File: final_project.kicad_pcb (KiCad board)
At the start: 2 copper layers, 21 parts, among them J1 Conn_01x04_Pin, U1 ATmega328-P, U2 SGP30, U3 TXS0102DCT, U3_5V_to_1.8V_Voltage_Regulator1 ADP3336ARMZ, U4 LM2576HVT-5, Y1 16 MHz

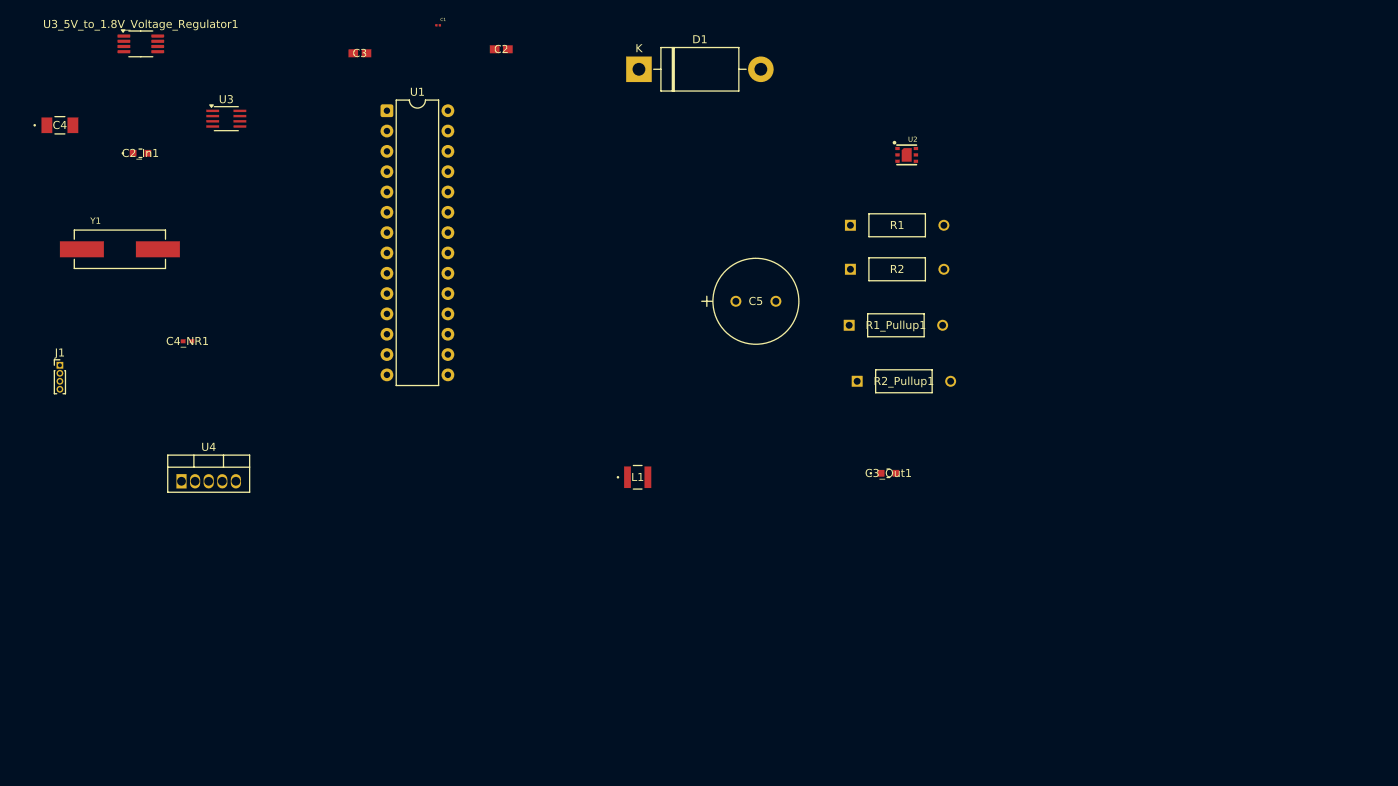
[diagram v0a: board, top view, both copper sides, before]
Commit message: Untangled PCB Design
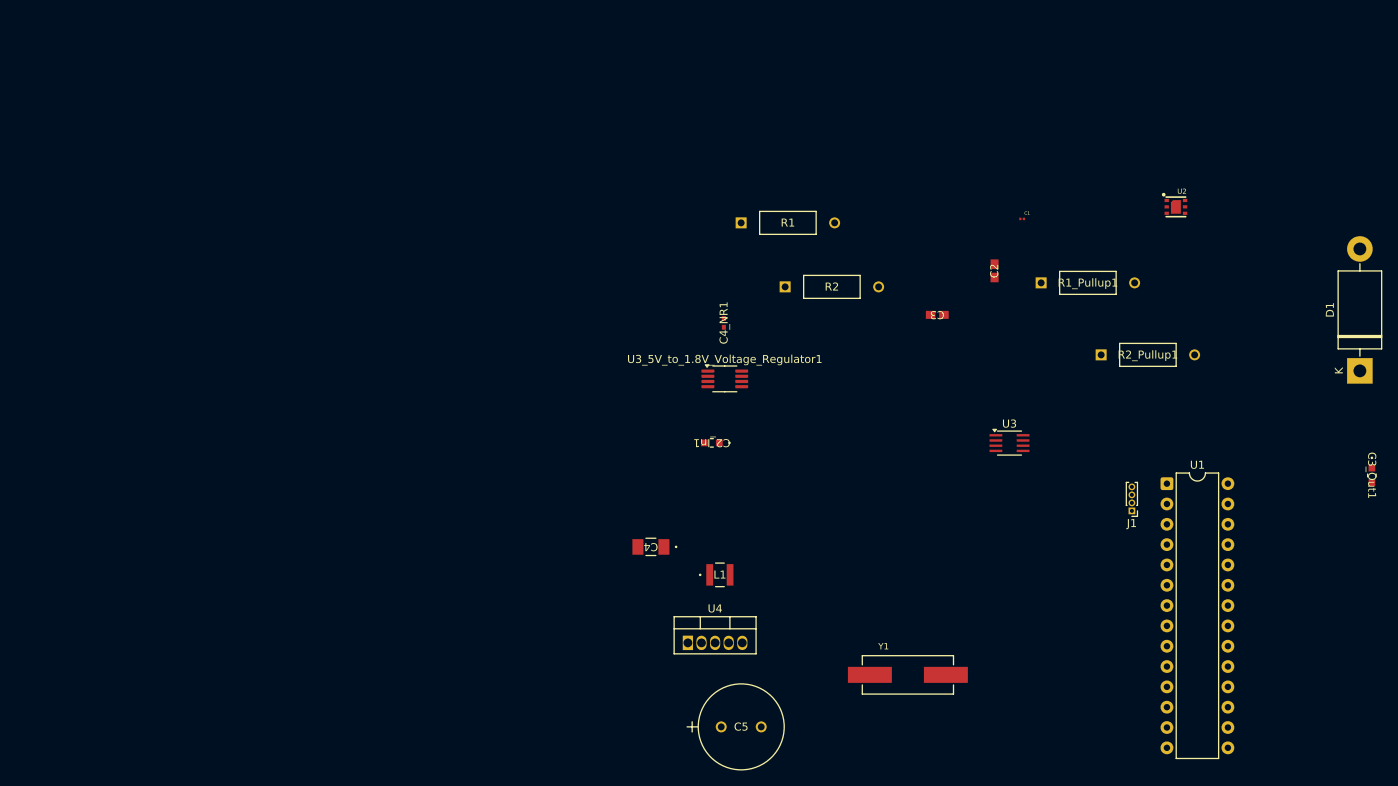
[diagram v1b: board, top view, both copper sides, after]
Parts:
- moved J1 135.2 mm to (150.5, 76.7), turned to 180 degrees
- moved Y1 111.9 mm to (122.5, 97.2)
- moved U1 108.1 mm to (154.9, 73.3)
- moved U3 106.0 mm to (135.2, 68.2)
- moved D1 97.7 mm to (179.0, 59.2), turned to 90 degrees
- moved C4 90.7 mm to (90.4, 81.2), turned to 180 degrees
- moved U3_5V_to_1.8V_Voltage_Regulator1 84.2 mm to (99.6, 60.2)
- moved C2_In1 80.1 mm to (98.0, 68.2), turned to 180 degrees
- moved C3 79.2 mm to (126.2, 52.2), turned to 180 degrees
- moved C1 76.9 mm to (136.8, 40.2)
- moved C2 67.6 mm to (133.3, 46.7), turned to 90 degrees
- moved C4_NR1 67.1 mm to (99.5, 53.2), turned to 90 degrees
- moved U4 66.4 mm to (95.0, 93.2)
- moved C3_Out1 60.4 mm to (180.5, 72.3), turned to -90 degrees
- moved C5 53.2 mm to (99.2, 103.7)
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
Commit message: Wire Connections to PCB
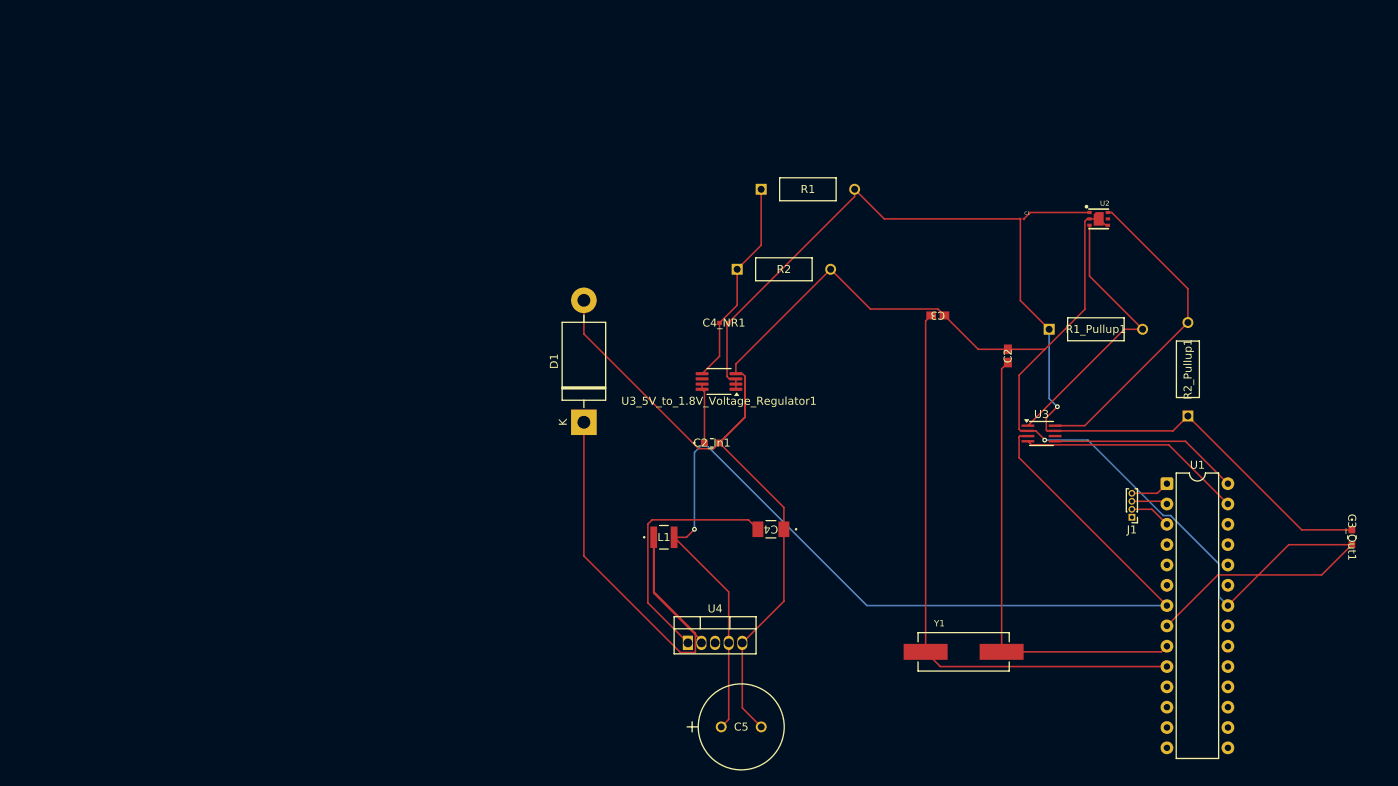
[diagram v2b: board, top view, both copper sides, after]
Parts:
- moved D1 97.2 mm to (82.0, 65.6)
- moved C4 15.2 mm to (105.4, 79.0)
- moved R2_Pullup1 13.3 mm to (157.5, 64.8), turned to 90 degrees
- moved C2 10.8 mm to (135.0, 57.3)
- moved U2 9.77 mm to (146.3, 40.2)
- moved L1 8.43 mm to (92.0, 80.0)
- moved C3_Out1 8.12 mm to (178.0, 80.0)
- moved Y1 7.54 mm to (129.5, 94.3)
- moved R2 6.39 mm to (101.2, 46.5)
- moved R1_Pullup1 5.89 mm to (140.2, 54.0)
- moved R1 4.89 mm to (104.2, 36.5)
- moved U3 4.18 mm to (139.2, 67.0)
- moved J1 0.80 mm to (150.5, 77.5)
- moved U3_5V_to_1.8V_Voltage_Regulator1 0.79 mm to (98.9, 60.5), turned to 180 degrees
- moved C3 0.09 mm to (126.2, 52.3)
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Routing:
- net GND: track 0.00 -> 255.2 mm, vias 0 -> 1
- net VCCA: track 0.00 -> 144.8 mm, vias 0 -> 1
- net VCCB: track 0.00 -> 128.6 mm, vias 0 -> 1
- net Net-(U1-XTAL2/PB7): track 0.00 -> 73.3 mm
- net Net-(D1-K): track 0.00 -> 67.9 mm
- net Net-(U1-XTAL1/PB6): track 0.00 -> 57.4 mm
- net SCL_2: track 0.00 -> 40.1 mm
- net SDA_2: track 0.00 -> 35.1 mm
- net +9V: track 0.00 -> 31.4 mm
- net SDA_1: track 0.00 -> 28.2 mm
- net Net-(U3_5V_to_1.8V_Voltage_Regulator1-FB): track 0.00 -> 26.1 mm
- net SCL_1: track 0.00 -> 23.8 mm
- net Net-(U2-VDD): track 0.00 -> 8.53 mm
- net Net-(J1-Pin_2): track 0.00 -> 5.16 mm
- net Net-(J1-Pin_4): track 0.00 -> 4.88 mm
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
